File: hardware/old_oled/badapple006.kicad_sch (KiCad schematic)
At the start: 35 parts, among them J10 5V, J11 GND, J12 RB066-6448-TSWHG01, J2 USB_C_Receptacle_USB2.0, J3 PG, J4 3v3, J5 GND, J6 RFO, J7 RFA, J8 APPLE, J9 RFO2, U1 CH32V006F8U7, U2 XC6206P332, Y1 24MHz

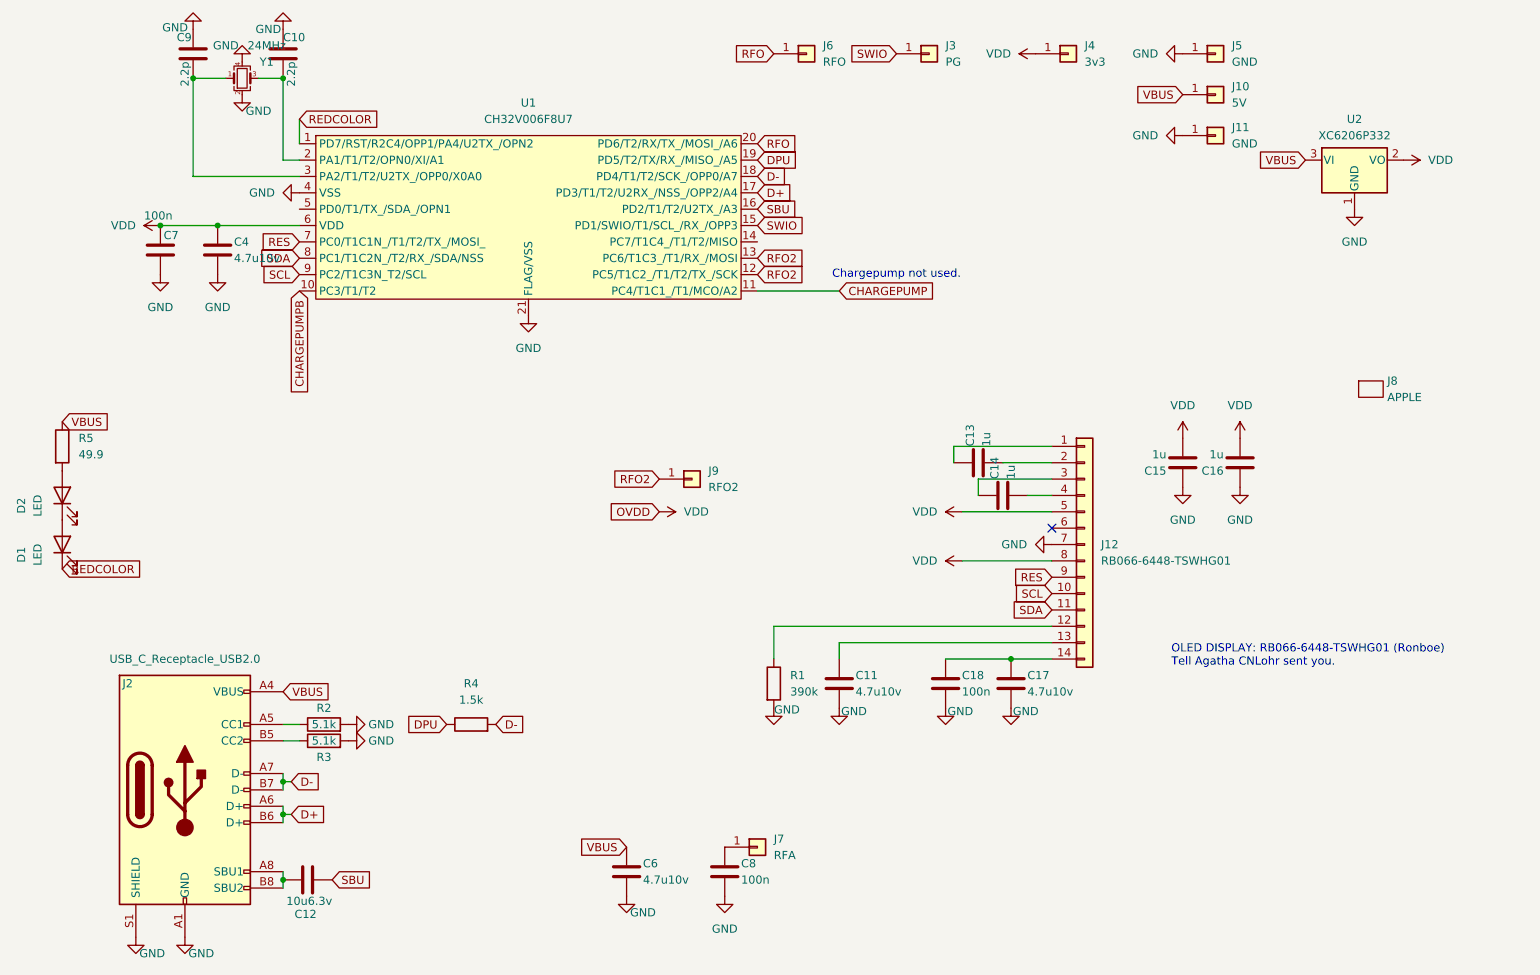
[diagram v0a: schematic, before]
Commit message: Update design for new Ronbo OLED
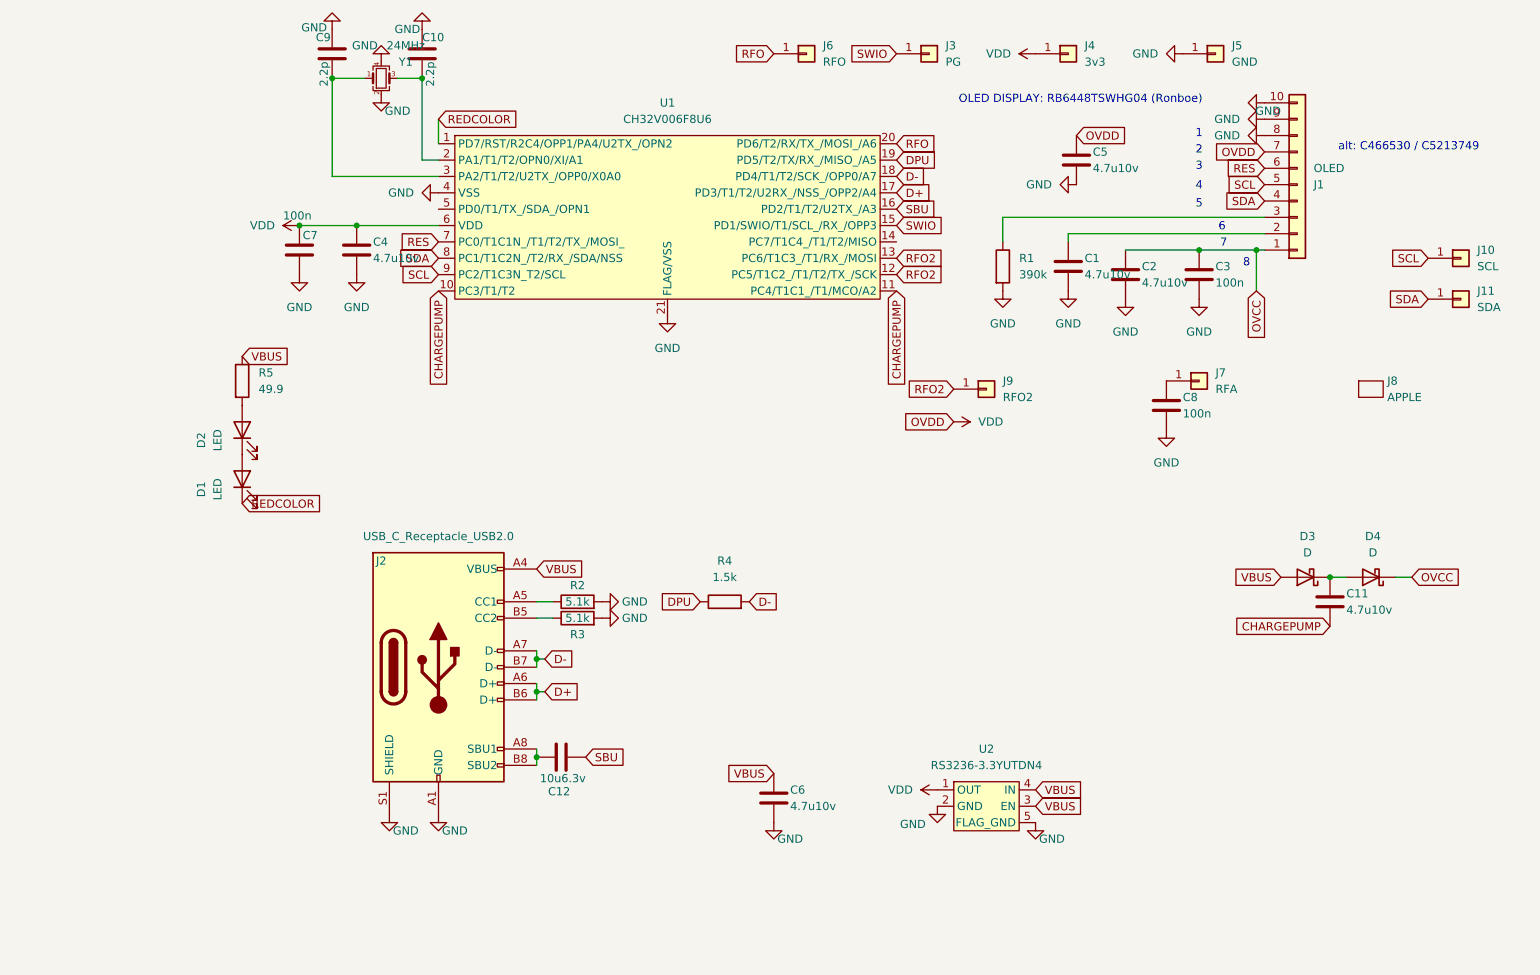
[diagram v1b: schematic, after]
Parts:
- removed C13, C14, C15, C16: 1u, Capacitor_SMD:C_0402_1005Metric, symbol Device:C
- removed C17: 4.7u10v, Capacitor_SMD:C_0402_1005Metric, symbol Device:C
- removed C18: 100n, Capacitor_SMD:C_0402_1005Metric, symbol Device:C
- removed J12: RB066-6448-TSWHG01, cnhardware:OLED-RB066-6448TSWHG01, symbol Connector_Generic:Conn_01x14
- removed U2: XC6206P332, Package_TO_SOT_SMD:SOT-23, symbol Regulator_Linear:AZ1117-5.0
- added C1, C2, C5: 4.7u10v, Capacitor_SMD:C_0402_1005Metric, symbol Device:C
- added C3: 100n, Capacitor_SMD:C_0402_1005Metric, symbol Device:C
- added D3, D4: D, Diode_SMD:D_SOD-323, symbol Device:D_Schottky
- added J1: OLED, fpc:AFC42-S08FMA-1H, symbol Connector_Generic:Conn_01x10
- added U2: RS3236-3.3YUTDN4, cnhardware:xdfn-reg, symbol cnhardware:RS3236-DFN-LDO
- J10: value 5V -> SCL
- J11: value GND -> SDA
- J2: footprint cnhardware:USB_C_TIGHT_IN_BOARD_161N-4BC21665 -> Connector_USB:USB_C_Receptacle_HRO_TYPE-C-31-M-12
- U1: value CH32V006F8U7 -> CH32V006F8U6; LCSC C55112440 -> C42431288
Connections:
- net CHARGEPUMPB is gone; now on net CHARGEPUMP: U1.10 (PC3/T1/T2)
- net CHARGEPUMP: now also C11.2
- net GND: now also C1.2, C2.2, C3.2, C5.2, J1.10 (Pin_10), J1.8 (Pin_8), J1.9 (Pin_9), U2.2 (GND), U2.5 (FLAG_GND); no longer C11.2, J11.1 (Pin_1)
- net RES: now also J1.6 (Pin_6)
- net SCL: now also J10.1 (Pin_1), J1.5 (Pin_5)
- net SDA: now also J11.1 (Pin_1), J1.4 (Pin_4)
- net VBUS: now also D3.2 (A), U2.3 (EN), U2.4 (IN); no longer J10.1 (Pin_1)
- net VDD: now also C5.1, J1.7 (Pin_7), U2.1 (OUT)
- net at C11.1: now also D3.1 (K), D4.2 (A)
- net at R1.1: now also J1.3 (Pin_3)
- new net: C1.1, J1.2 (Pin_2)
- new net OVCC: C2.1, C3.1, D4.1 (K), J1.1 (Pin_1)
- no-connect marks 1 -> 0
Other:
- note added: "1"
- note added: "2"
- note added: "3"
- note added: "4"
- note added: "5"
- note added: "6"
- note added: "7"
- note added: "8"
- note added: "OLED DISPLAY: RB6448TSWHG04 (Ronboe)"
- note added: "alt: C466530 / C5213749"
- note removed: "Chargepump not used."
- note removed: "OLED DISPLAY: RB066-6448-TSWHG01 (Ronboe) Tell Agatha CNLohr sent you."
- moved on the sheet: C10, C12, C4, C6, C7, C8, C9, D1, D2, J2, J7, J9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
